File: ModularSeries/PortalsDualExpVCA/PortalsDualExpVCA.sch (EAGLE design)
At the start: 71 parts, among them Q1 2N3906, Q2 2N3906, Q3 2N3906, Q4 2N3906

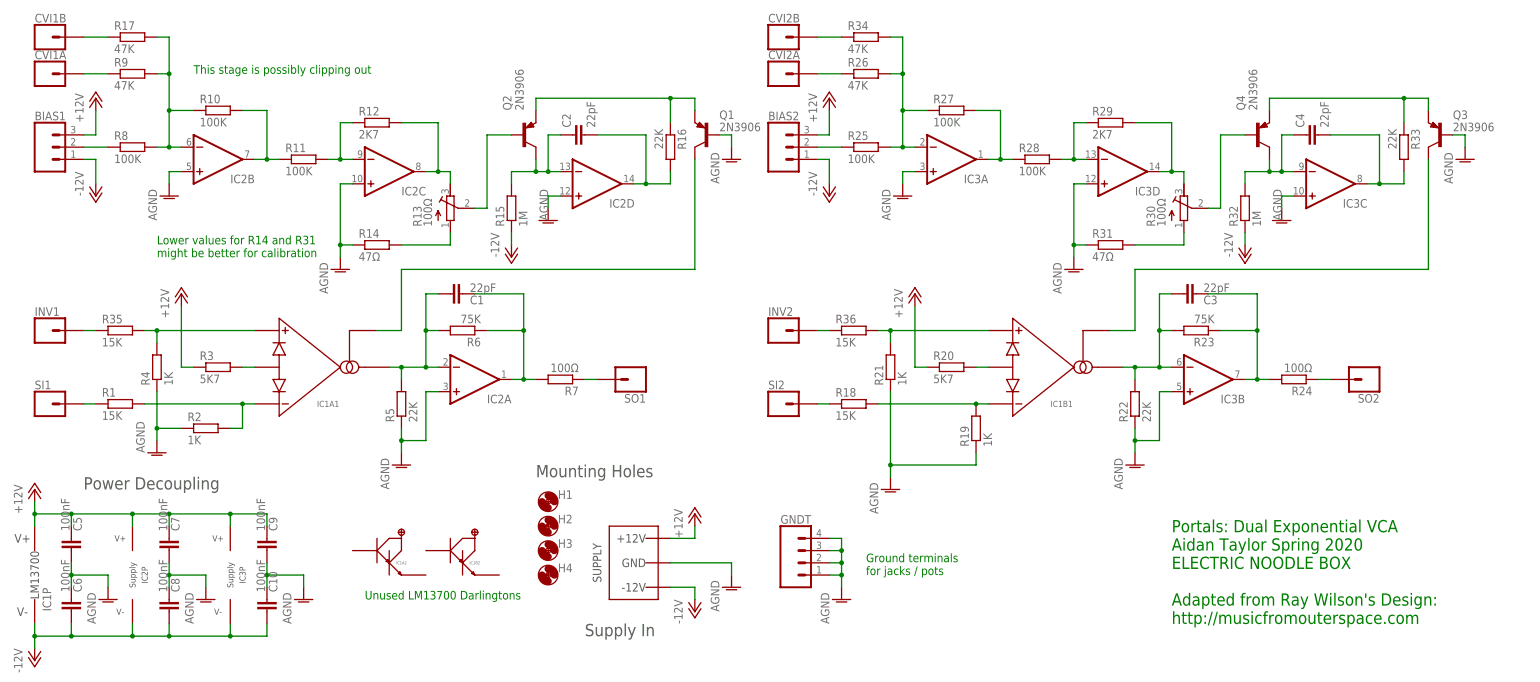
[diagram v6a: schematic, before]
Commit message: Layout and schematic renders for LHP added
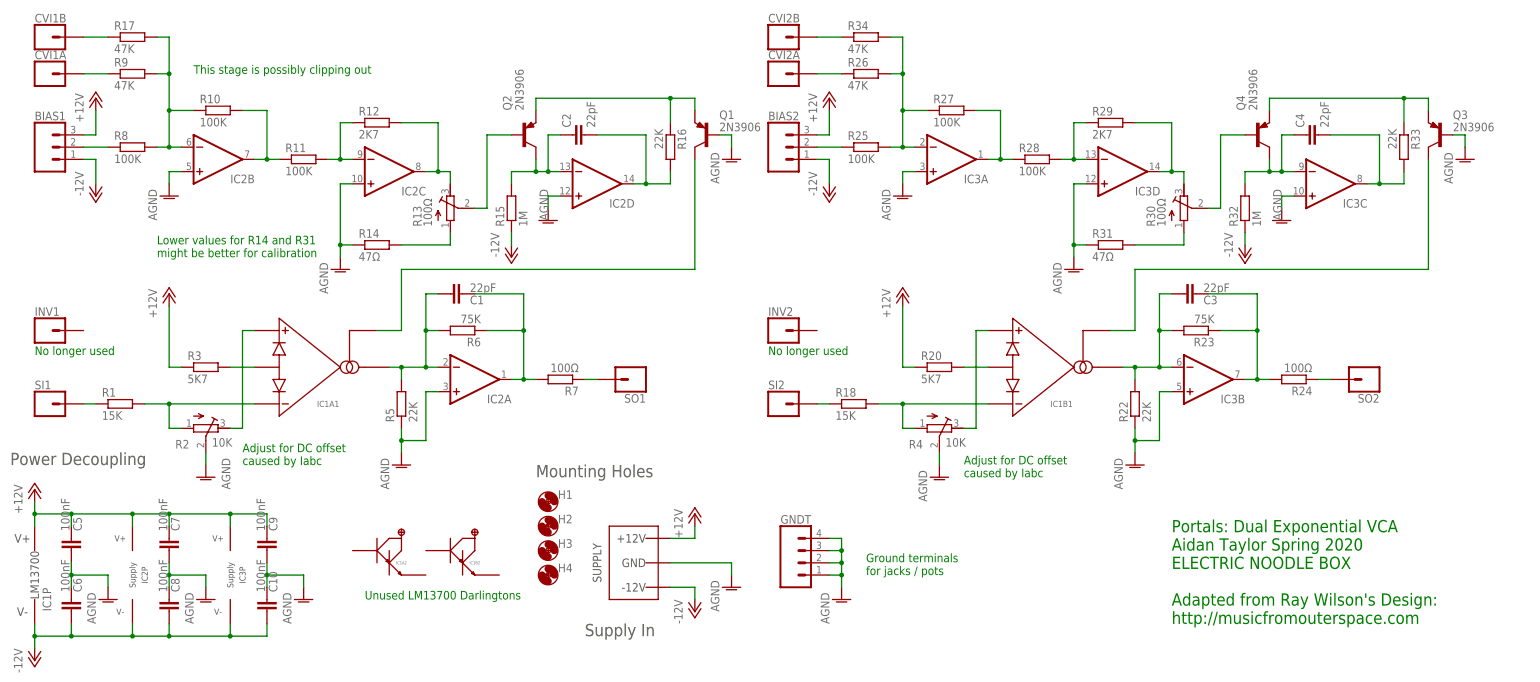
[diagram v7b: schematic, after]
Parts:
- removed R19, R21: 1K, rcl:R-EU_0207/10
- removed R35, R36: 15K, rcl:R-EU_0207/10
- R2, R4: value 1K -> 10K; device rcl:R-EU_0207/10 -> rcl:R-TRIMM3296W
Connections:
- removed net N$41: INV1.1, R35.1
- removed net N$42: INV2.1, R36.1
- net AGND: now also R2.S, R4.S; no longer R19.1, R2.1, R21.1, R4.1
- net N$2: now also R2.E; no longer R35.2, R4.2
- net N$22: now also R4.E; no longer R21.2, R36.2
- net N$23: now also R4.A; no longer R19.2
- net N$4: now also R2.A; no longer R2.2
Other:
- note added: "Adjust for DC offset caused by Iabc"
- note added: "No longer used"
- moved on the sheet: R20, R3

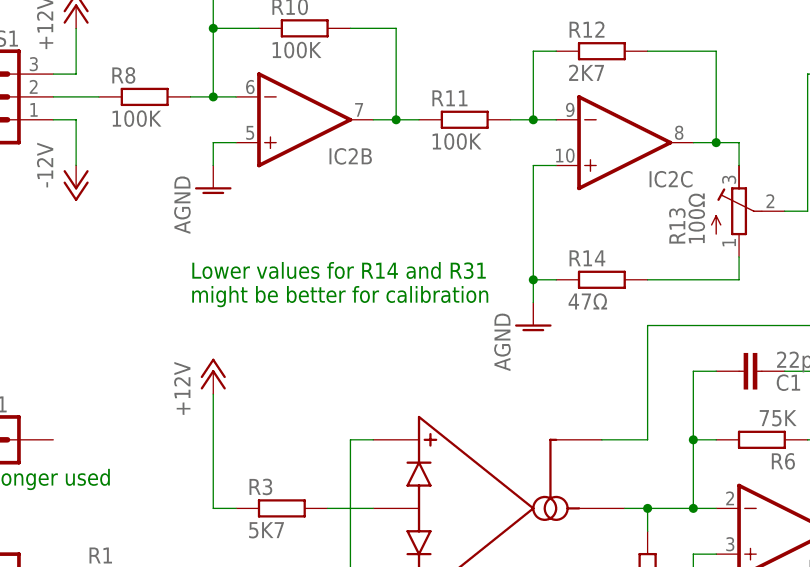
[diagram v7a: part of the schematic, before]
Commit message: Formula updates added
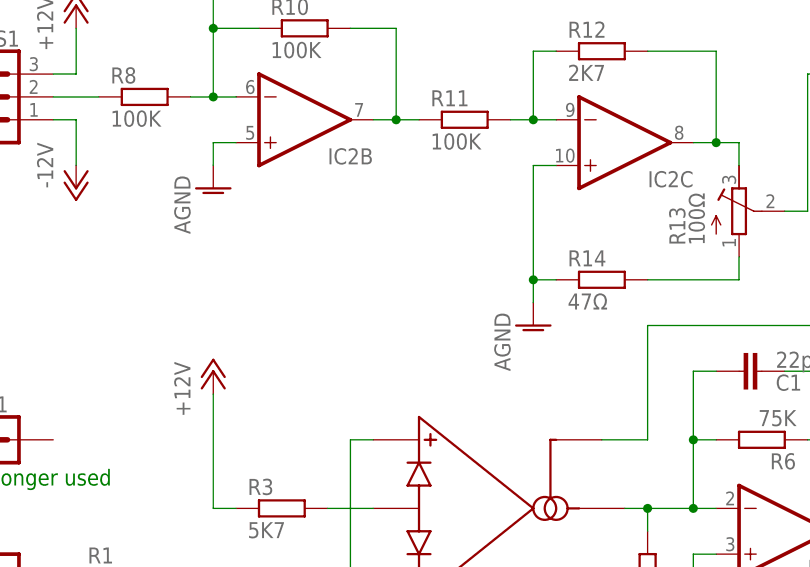
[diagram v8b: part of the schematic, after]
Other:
- note removed: "Lower values for R14 and R31 might be better for calibration"
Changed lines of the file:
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@@
 <text x="177.8" y="22.86" size="1.778" layer="91">Ground terminals
 for jacks / pots</text>
-<text x="30.48" y="88.9" size="1.778" layer="91">Lower values for R14 and R31
-might be better for calibration</text>
 <text x="38.1" y="127" size="1.778" layer="91">This stage is possibly clipping out</text>
 <text x="5.08" y="68.58" size="1.778" layer="91">No longer used</text>
